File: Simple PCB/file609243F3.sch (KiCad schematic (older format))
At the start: 25 parts, among them J26 Motor Left, J27 Cutter Motor, J28 Motor Right, U1 MC33926, U2 MC33926

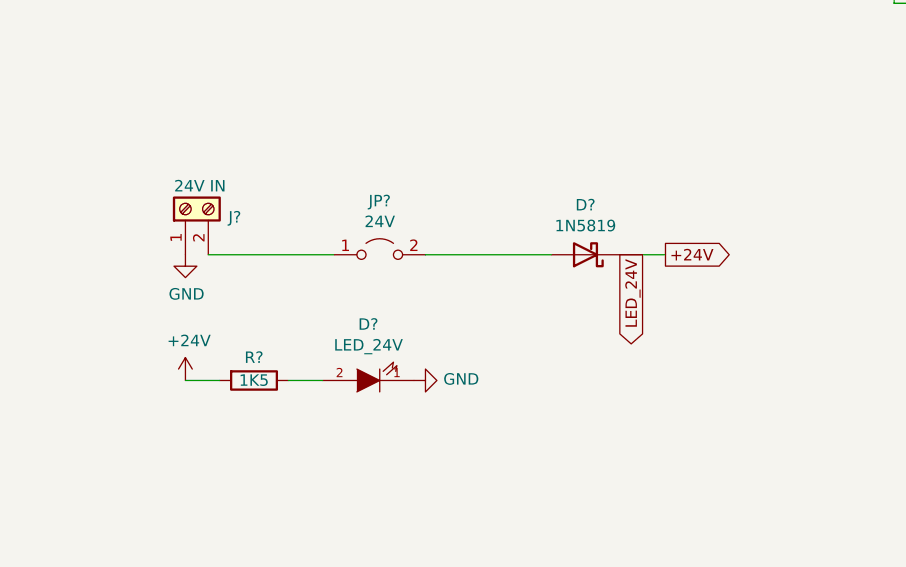
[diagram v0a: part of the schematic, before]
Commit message: Starsurfer78
Sorting the Footprints on PCB
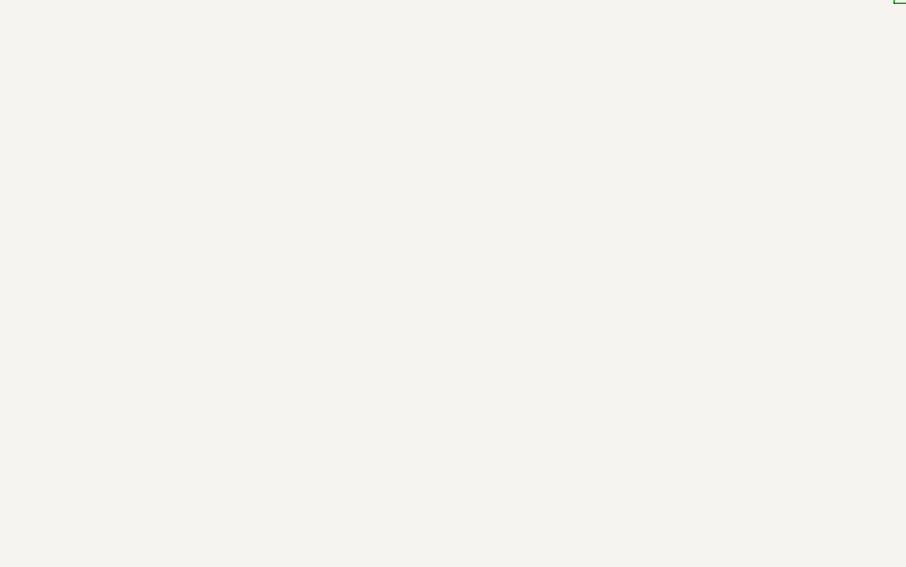
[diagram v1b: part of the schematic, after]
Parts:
- removed D?: LED_24V, LED_THT:LED_D3.0mm, symbol Zimprich:LED
- removed D?: 1N5819, Diode_THT:D_DO-41_SOD81_P10.16mm_Horizontal, symbol Diode:1N5819
- removed J?: 24V IN, TerminalBlock:TerminalBlock_bornier-2_P5.08mm, symbol Connector:Screw_Terminal_01x02
- removed JP?: 24V, Connector_PinSocket_2.54mm:PinSocket_1x02_P2.54mm_Vertical, symbol Jumper:Jumper_2_Open
- removed R?: 1K5, Resistor_THT:R_Axial_DIN0207_L6.3mm_D2.5mm_P2.54mm_Vertical, symbol Device:R
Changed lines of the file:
@@
 Wire Wire Line
 	4100 6150 4200 6150
-$Comp
-L Device:R R?
-U 1 1 6096C7A3
-P 5750 4000
-F 0 "R?" V 5650 4000 50  0000 C CNN
-F 1 "1K5" V 5750 4000 50  0000 C CNN
-F 2 "Resistor_THT:R_Axial_DIN0207_L6.3mm_D2.5mm_P2.54mm_Vertical" V 5680 4000 50  0001 C CNN
-F 3 "~" H 5750 4000 50  0001 C CNN
-	1    5750 4000
-	0    1    1    0
-$EndComp
-$Comp
-L power:+24V #PWR?
-U 1 1 6096C7A9
-P 5450 4000
-F 0 "#PWR?" H 5450 3850 50  0001 C CNN
-F 1 "+24V" H 5465 4173 50  0000 C CNN
-F 2 "" H 5450 4000 50  0001 C CNN
-F 3 "" H 5450 4000 50  0001 C CNN
-	1    5450 4000
-	1    0    0    -1
-$EndComp
-Wire Wire Line
-	5450 4000 5600 4000
-Wire Wire Line
-	5900 4000 6050 4000
-$Comp
-L power:GND #PWR?
-U 1 1 6096C7B1
-P 6450 4000
-F 0 "#PWR?" H 6450 3750 50  0001 C CNN
-F 1 "GND" V 6455 3872 50  0000 R CNN
-F 2 "" H 6450 4000 50  0001 C CNN
-F 3 "" H 6450 4000 50  0001 C CNN
-	1    6450 4000
-	0    -1   -1   0
-$EndComp
-$Comp
-L Zimprich:LED D?
-U 1 1 6096C7B7
-P 6250 4000
-F 0 "D?" H 6250 3755 50  0000 C CNN
-F 1 "LED_24V" H 6250 3846 50  0000 C CNN
-F 2 "LED_THT:LED_D3.0mm" H 6250 4000 60  0001 C CNN
-F 3 "" H 6250 4000 60  0000 C CNN
-	1    6250 4000
-	-1   0    0    1
-$EndComp
-$Comp
-L Jumper:Jumper_2_Open JP?
-U 1 1 6096C7BD
-P 6300 3450
-F 0 "JP?" H 6300 3685 50  0000 C CNN
-F 1 "24V" H 6300 3594 50  0000 C CNN
-F 2 "Connector_PinSocket_2.54mm:PinSocket_1x02_P2.54mm_Vertical" H 6300 3450 50  0001 C CNN
-F 3 "~" H 6300 3450 50  0001 C CNN
-	1    6300 3450
-	1    0    0    -1
-$EndComp
-$Comp
-L Connector:Screw_Terminal_01x02 J?
-U 1 1 6096C7C3
-P 5450 3250
-F 0 "J?" V 5414 3062 50  0000 R CNN
-F 1 "24V IN" V 5550 3300 50  0000 R CNN
-F 2 "TerminalBlock:TerminalBlock_bornier-2_P5.08mm" H 5450 3250 50  0001 C CNN
-F 3 "~" H 5450 3250 50  0001 C CNN
-	1    5450 3250
-	0    -1   -1   0
-$EndComp
-$Comp
-L Diode:1N5819 D?
-U 1 1 6096C7C9
-P 7200 3450
-F 0 "D?" H 7200 3233 50  0000 C CNN
-F 1 "1N5819" H 7200 3324 50  0000 C CNN
-F 2 "Diode_THT:D_DO-41_SOD81_P10.16mm_Horizontal" H 7200 3275 50  0001 C CNN
-F 3 "http://www.vishay.com/docs/88525/1n5817.pdf" H 7200 3450 50  0001 C CNN
-	1    7200 3450
-	-1   0    0    1
-$EndComp
-Text GLabel 7550 3450 2    50   Output ~ 0
-+24V
-Wire Wire Line
-	6500 3450 7050 3450
-Wire Wire Line
-	5550 3450 6100 3450
-$Comp
-L power:GND #PWR?
-U 1 1 6096C7D2
-P 5450 3450
-F 0 "#PWR?" H 5450 3200 50  0001 C CNN
-F 1 "GND" H 5455 3277 50  0000 C CNN
-F 2 "" H 5450 3450 50  0001 C CNN
-F 3 "" H 5450 3450 50  0001 C CNN
-	1    5450 3450
-	1    0    0    -1
-$EndComp
-Wire Wire Line
-	7350 3450 7550 3450
-Text GLabel 7400 3450 3    50   Output ~ 0
-LED_24V
 $EndSCHEMATC
